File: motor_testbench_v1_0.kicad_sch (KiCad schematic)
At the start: 22 parts, among them J1 Conn_01x05_Pin, J2 Conn_01x01_Pin, J3 Conn_01x01_Pin, J4 Conn_01x22_Pin, U1 ESP32-S3-DevKitC

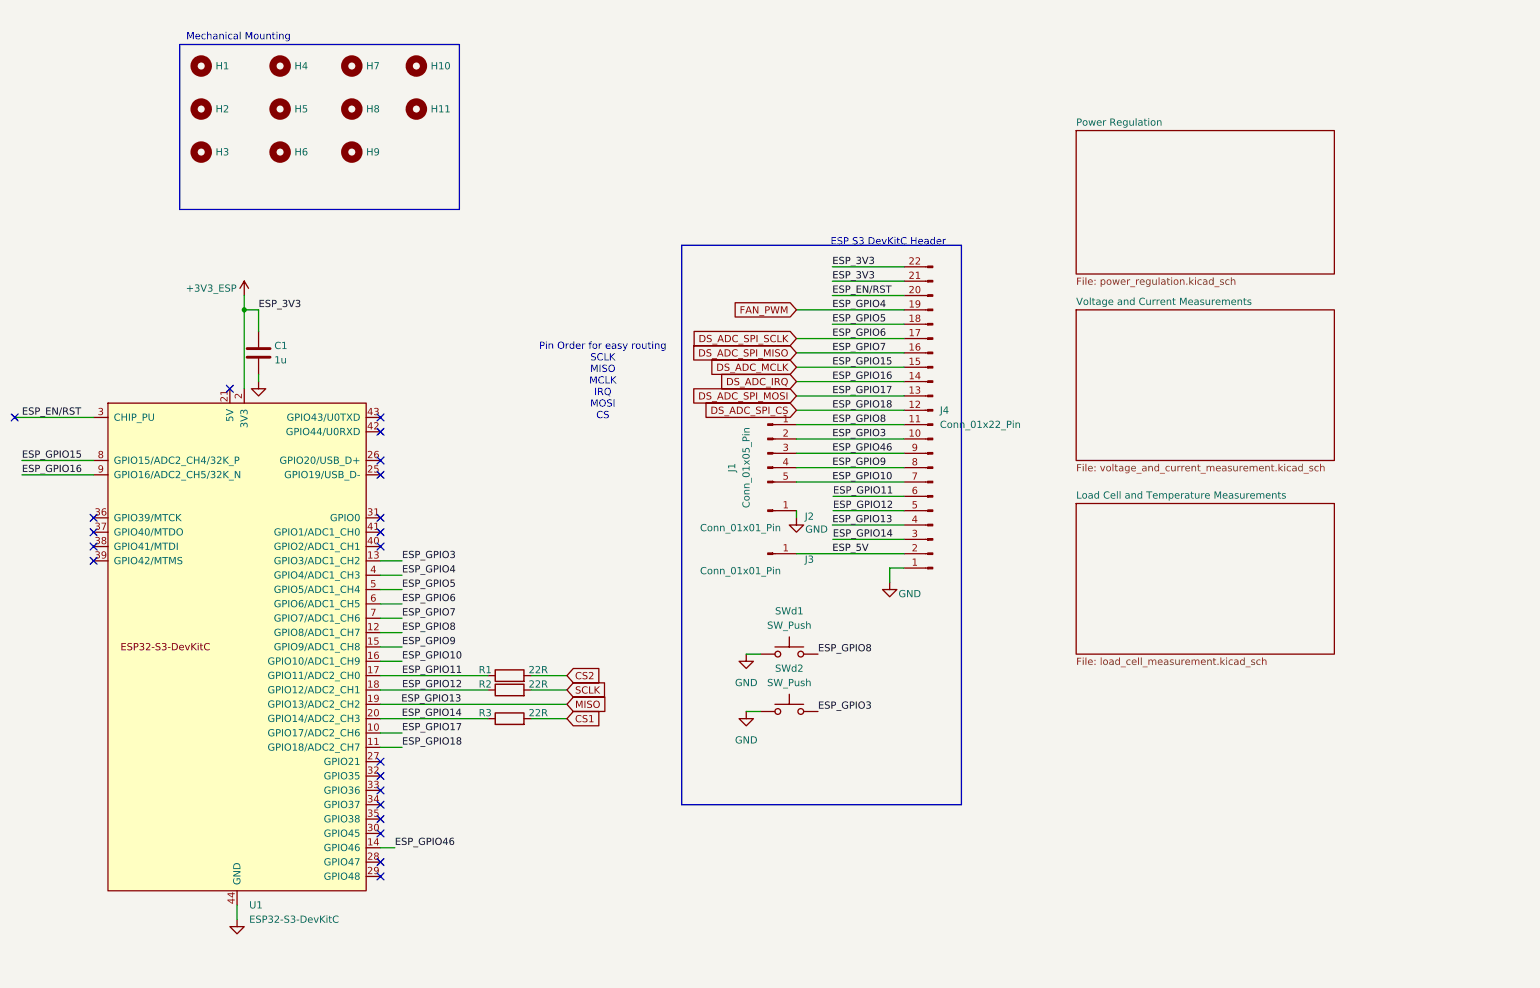
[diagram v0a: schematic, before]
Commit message: Implemented SAR ADC Buffering on top layer with one OPA387
[KiCad Version: 10.0.4]
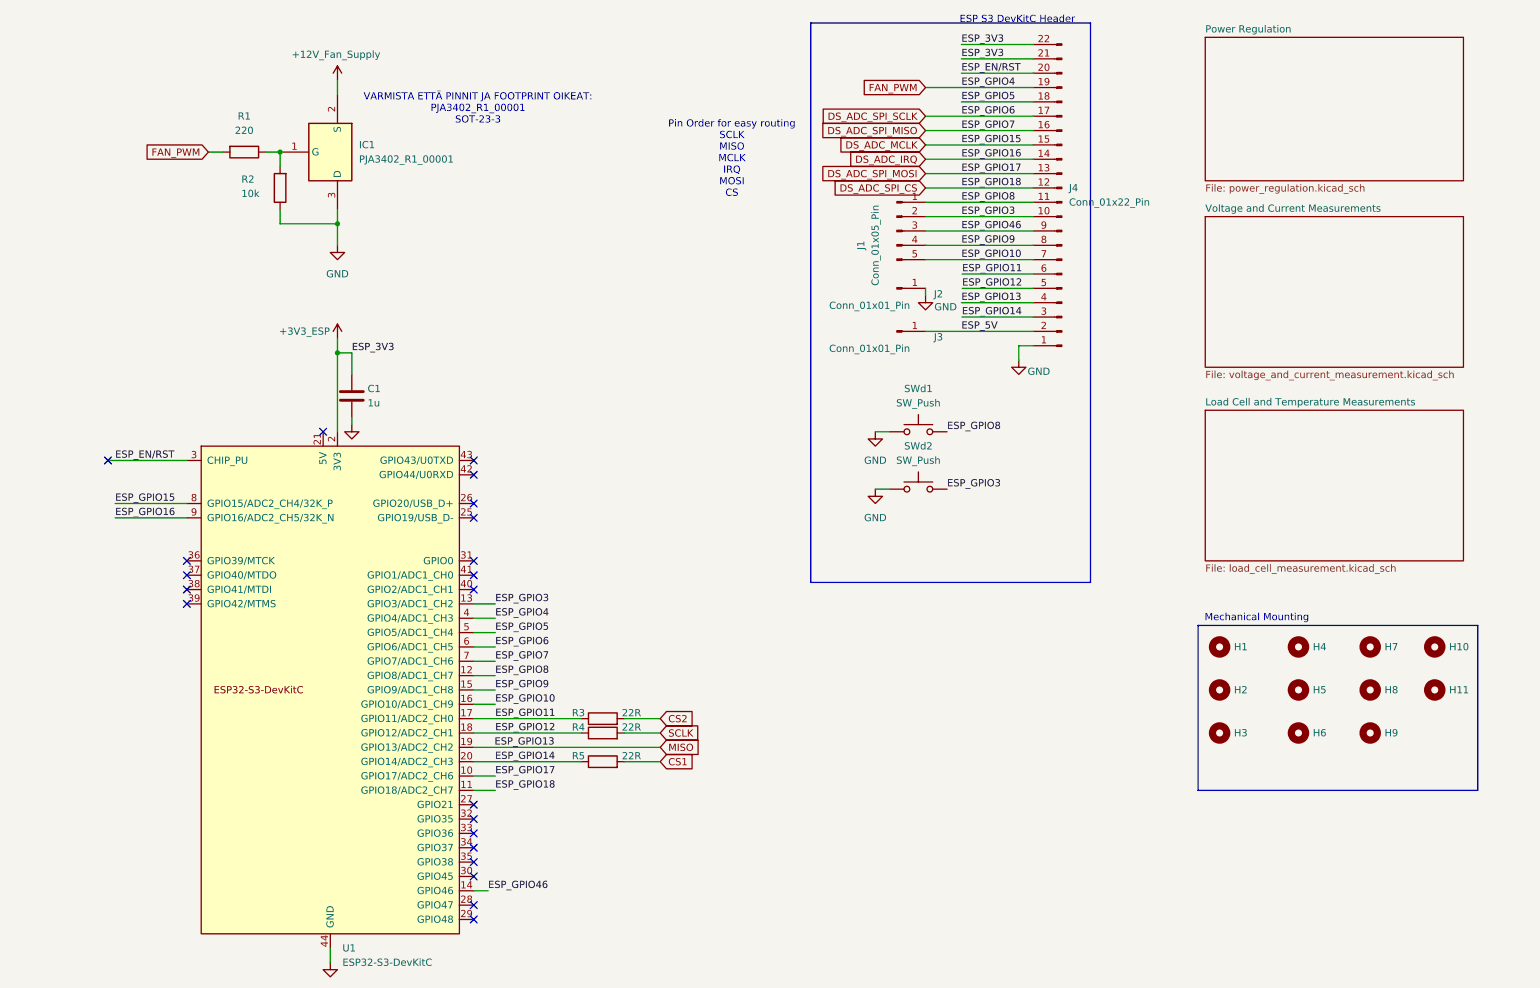
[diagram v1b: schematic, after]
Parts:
- added IC1: PJA3402_R1_00001, SOT95P240X110-3N, symbol SamacSys_Parts:PJA3402_R1_00001
- added R1: 220, Resistor_SMD:R_0603_1608Metric_Pad0.98x0.95mm_HandSolder, symbol Device:R
- added R2: 10k, Resistor_SMD:R_0603_1608Metric_Pad0.98x0.95mm_HandSolder, symbol Device:R
- renumbered R1 to R3, R2 to R4, R3 to R5
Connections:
- net FAN_PWM: now also R1.2
- net GND: now also IC1.3 (D), R2.1
- new net: IC1.1 (G), R1.1, R2.2
- new net +12V_Fan_Supply: IC1.2 (S)
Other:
- note added: "VARMISTA ETTÄ PINNIT JA FOOTPRINT OIKEAT: PJA3402_R1_00001 SOT-23-3"
- moved on the sheet: C1, H1, H10, H11, H2, H3, H4, H5, H6, H7, H8, H9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

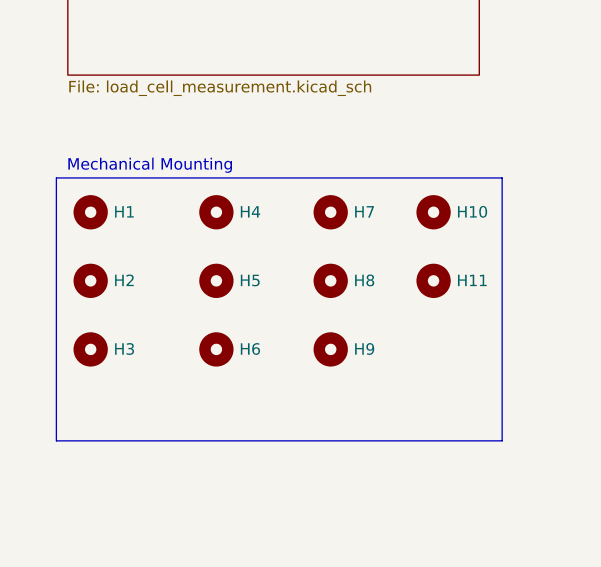
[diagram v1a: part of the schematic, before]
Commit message: Add Shutdown Protection Diodes between Power Stages
[KiCad Version: 10.0.4]
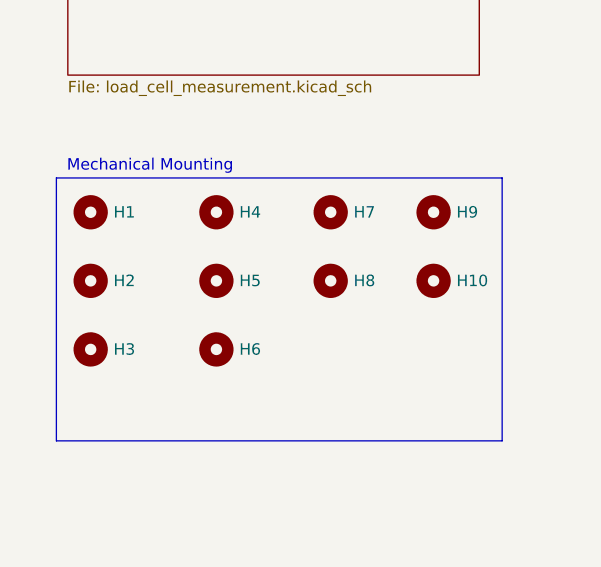
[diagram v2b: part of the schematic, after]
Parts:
- removed H4: MountingHole, MountingHole:MountingHole_2.2mm_M2_DIN965, symbol Mechanical:MountingHole
- renumbered H11 to H10, H9 to H4, H10 to H9
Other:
- moved on the sheet: H4
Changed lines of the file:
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@@
 		(in_pos_files yes)
 		(dnp no)
-		(property "Reference" "H11"
+		(property "Reference" "H10"
 			(at 275.59 137.16 0)
 			(show_name no)
@@
 			(project "motor_testbench_v1_0"
 				(path "/da638649-102c-44f9-b928-e91cd399cc2f"
-					(reference "H11")
+					(reference "H10")
 					(unit 1)
 				)
@@
 		(in_pos_files yes)
 		(dnp no)
-		(property "Reference" "H10"
+		(property "Reference" "H9"
 			(at 275.59 129.54 0)
 			(show_name no)
@@
 			(project "motor_testbench_v1_0"
 				(path "/da638649-102c-44f9-b928-e91cd399cc2f"
-					(reference "H10")
+					(reference "H9")
 					(unit 1)
 				)
@@
 					(unit 1)
 				)
-			)
-		)
-	)
-	(symbol
-		(lib_id "Mechanical:MountingHole")
-		(at 261.62 144.78 0)
-		(unit 1)
-		(body_style 1)
-		(exclude_from_sim no)
-		(in_bom no)
-		(on_board yes)
-		(in_pos_files yes)
-		(dnp no)
-		(property "Reference" "H9"
-			(at 264.16 144.78 0)
-			(show_name no)
-			(do_not_autoplace no)
-			(effects
-				(font
-					(size 1.27 1.27)
-				)
-				(justify left)
-			)
-		)
-		(property "Value" "MountingHole"
-			(at 264.16 146.0499 0)
-			(hide yes)
-			(show_name no)
-			(do_not_autoplace no)
-			(effects
-				(font
-					(size 1.27 1.27)
-				)
-				(justify left)
-			)
-		)
-		(property "Footprint" "MountingHole:MountingHole_2.2mm_M2_DIN965"
-			(at 261.62 144.78 0)
-			(hide yes)
-			(show_name no)
-			(do_not_autoplace no)
-			(effects
-				(font
-					(size 1.27 1.27)
-				)
-			)
-		)
-		(property "Datasheet" ""
-			(at 261.62 144.78 0)
-			(hide yes)
-			(show_name no)
-			(do_not_autoplace no)
-			(effects
-				(font
-					(size 1.27 1.27)
-				)
-			)
-		)
-		(property "Description" "Mounting Hole without connection"
-			(at 261.62 144.78 0)
-			(hide yes)
-			(show_name no)
-			(do_not_autoplace no)
-			(effects
-				(font
-					(size 1.27 1.27)
-				)
-			)
-		)
-		(property "Manufacturing_Number" ""
-			(at 261.62 144.78 0)
-			(hide yes)
-			(show_name no)
-			(do_not_autoplace no)
-			(effects
-				(font
-					(size 1.27 1.27)
-				)
-			)
-		)
-		(instances
-			(project "motor_testbench_v1_0"
-				(path "/da638649-102c-44f9-b928-e91cd399cc2f"
-					(reference "H9")
-					(unit 1)
-				)

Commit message: Minor Tweaks.
[KiCad Version: 10.0.4]
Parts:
- added C2: 1u, Capacitor_SMD:C_0603_1608Metric_Pad1.08x0.95mm_HandSolder, symbol Device:C
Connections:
- net +3V3_ESP: now also C2.1
- net GND: now also C2.2
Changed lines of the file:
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@@
 		(color 0 0 0 0)
 	)
+	(junction
+		(at 81.28 77.47)
+		(diameter 0)
+		(color 0 0 0 0)
+	)
 	(no_connect
 		(at 102.87 175.26)
@@
 	(wire
 		(pts
+			(xy 88.9 88.9) (xy 88.9 90.17)
+		)
+		(stroke
+			(width 0)
+			(type default)
+		)
+	)
+	(wire
+		(pts
 			(xy 173.99 91.44) (xy 176.53 91.44)
 		)
@@
 	(wire
 		(pts
+			(xy 88.9 77.47) (xy 88.9 81.28)
+		)
+		(stroke
+			(width 0)
+			(type default)
+		)
+	)
+	(wire
+		(pts
 			(xy 102.87 121.92) (xy 106.68 121.92)
 		)
@@
 	(wire
 		(pts
+			(xy 81.28 77.47) (xy 88.9 77.47)
+		)
+		(stroke
+			(width 0)
+			(type default)
+		)
+	)
+	(wire
+		(pts
 			(xy 189.3177 71.12) (xy 201.93 71.12)
 		)
@@
 		(dnp no)
 		(fields_autoplaced yes)
-		(property "Reference" "#PWR07"
+		(property "Reference" "#PWR08"
 			(at 173.99 107.95 0)
 			(hide yes)
@@
 			(project "motor_testbench_v1_0"
 				(path "/da638649-102c-44f9-b928-e91cd399cc2f"
-					(reference "#PWR07")
+					(reference "#PWR08")
+					(unit 1)
+				)
+			)
+		)
+	)
+	(symbol
+		(lib_id "Device:C")
+		(at 88.9 85.09 0)
+		(unit 1)
+		(body_style 1)
+		(exclude_from_sim no)
+		(in_bom yes)
+		(on_board yes)
+		(in_pos_files yes)
+		(dnp no)
+		(property "Reference" "C2"
+			(at 91.694 83.82 0)
+			(show_name no)
+			(do_not_autoplace no)
+			(effects
+				(font
+					(size 1.27 1.27)
+				)
+				(justify left)
+			)
+		)
+		(property "Value" "1u"
+			(at 91.694 86.36 0)
+			(show_name no)
+			(do_not_autoplace no)
+			(effects
+				(font
+					(size 1.27 1.27)
+				)
+				(justify left)
+			)
+		)
+		(property "Footprint" "Capacitor_SMD:C_0603_1608Metric_Pad1.08x0.95mm_HandSolder"
+			(at 89.8652 88.9 0)
+			(hide yes)
+			(show_name no)
+			(do_not_autoplace no)
+			(effects
+				(font
+					(size 1.27 1.27)
+				)
+			)
+		)
+		(property "Datasheet" ""
+			(at 88.9 85.09 0)
+			(hide yes)
+			(show_name no)
+			(do_not_autoplace no)
+			(effects
+				(font
+					(size 1.27 1.27)
+				)
+			)
+		)
+		(property "Description" "Unpolarized capacitor"
+			(at 88.9 85.09 0)
+			(hide yes)
+			(show_name no)
+			(do_not_autoplace no)
+			(effects
+				(font
+					(size 1.27 1.27)
+				)
+			)
+		)
+		(property "Manufacturing_Number" ""
+			(at 88.9 85.09 0)
+			(hide yes)
+			(show_name no)
+			(do_not_autoplace no)
+			(effects
+				(font
+					(size 1.27 1.27)
+				)
+			)
+		)
+		(pin "2"
+		)
+		(pin "1"
+		)
+		(instances
+			(project "motor_testbench_v1_0"
+				(path "/da638649-102c-44f9-b928-e91cd399cc2f"
+					(reference "C2")
 					(unit 1)
 				)
@@
 		(in_pos_files yes)
 		(dnp no)
-		(property "Reference" "#PWR09"
+		(property "Reference" "#PWR010"
 			(at 199.39 85.09 0)
 			(hide yes)
@@
 			(project "motor_testbench_v1_0"
 				(path "/da638649-102c-44f9-b928-e91cd399cc2f"
-					(reference "#PWR09")
+					(reference "#PWR010")
 					(unit 1)
 				)
@@
 		(in_pos_files yes)
 		(dnp no)
-		(property "Reference" "#PWR08"
+		(property "Reference" "#PWR09"
 			(at 182.88 73.66 0)
 			(hide yes)
@@
 			(project "motor_testbench_v1_0"
 				(path "/da638649-102c-44f9-b928-e91cd399cc2f"
-					(reference "#PWR08")
+					(reference "#PWR09")
 					(unit 1)
 				)
@@
 		(dnp no)
 		(fields_autoplaced yes)
-		(property "Reference" "#PWR06"
+		(property "Reference" "#PWR07"
 			(at 173.99 97.79 0)
 			(hide yes)
@@
 			(project "motor_testbench_v1_0"
 				(path "/da638649-102c-44f9-b928-e91cd399cc2f"
-					(reference "#PWR06")
+					(reference "#PWR07")
 					(unit 1)
 				)
@@
 					(unit 1)
 				)
+			)
+		)
+	)
+	(symbol
+		(lib_id "power:GND")
+		(at 88.9 90.17 0)
+		(unit 1)
+		(body_style 1)
+		(exclude_from_sim no)
+		(in_bom yes)
+		(on_board yes)
+		(in_pos_files yes)
+		(dnp no)
+		(fields_autoplaced yes)
+		(property "Reference" "#PWR06"
+			(at 88.9 96.52 0)
+			(hide yes)
+			(show_name no)
+			(do_not_autoplace no)
+			(effects
+				(font
+					(size 1.27 1.27)
+				)
+			)
+		)
+		(property "Value" "GND"
+			(at 88.9 95.25 0)
+			(hide yes)
+			(show_name no)
+			(do_not_autoplace no)
+			(effects
+				(font
+					(size 1.27 1.27)
+				)
+			)
+		)
+		(property "Footprint" ""
+			(at 88.9 90.17 0)
+			(hide yes)
+			(show_name no)
+			(do_not_autoplace no)
+			(effects
+				(font
+					(size 1.27 1.27)
+				)
+			)
+		)
+		(property "Datasheet" ""
+			(at 88.9 90.17 0)
+			(hide yes)
+			(show_name no)
+			(do_not_autoplace no)
+			(effects
+				(font
+					(size 1.27 1.27)
+				)
+			)
+		)
+		(property "Description" "Power symbol creates a global label with name \"GND\" , ground"
+			(at 88.9 90.17 0)
+			(hide yes)
+			(show_name no)
+			(do_not_autoplace no)
+			(effects
+				(font
+					(size 1.27 1.27)
+				)
+			)
+		)
+		(pin "1"
+		)
+		(instances
+			(project "motor_testbench_v1_0"
+				(path "/da638649-102c-44f9-b928-e91cd399cc2f"
+					(reference "#PWR06")
+					(unit 1)
+				)

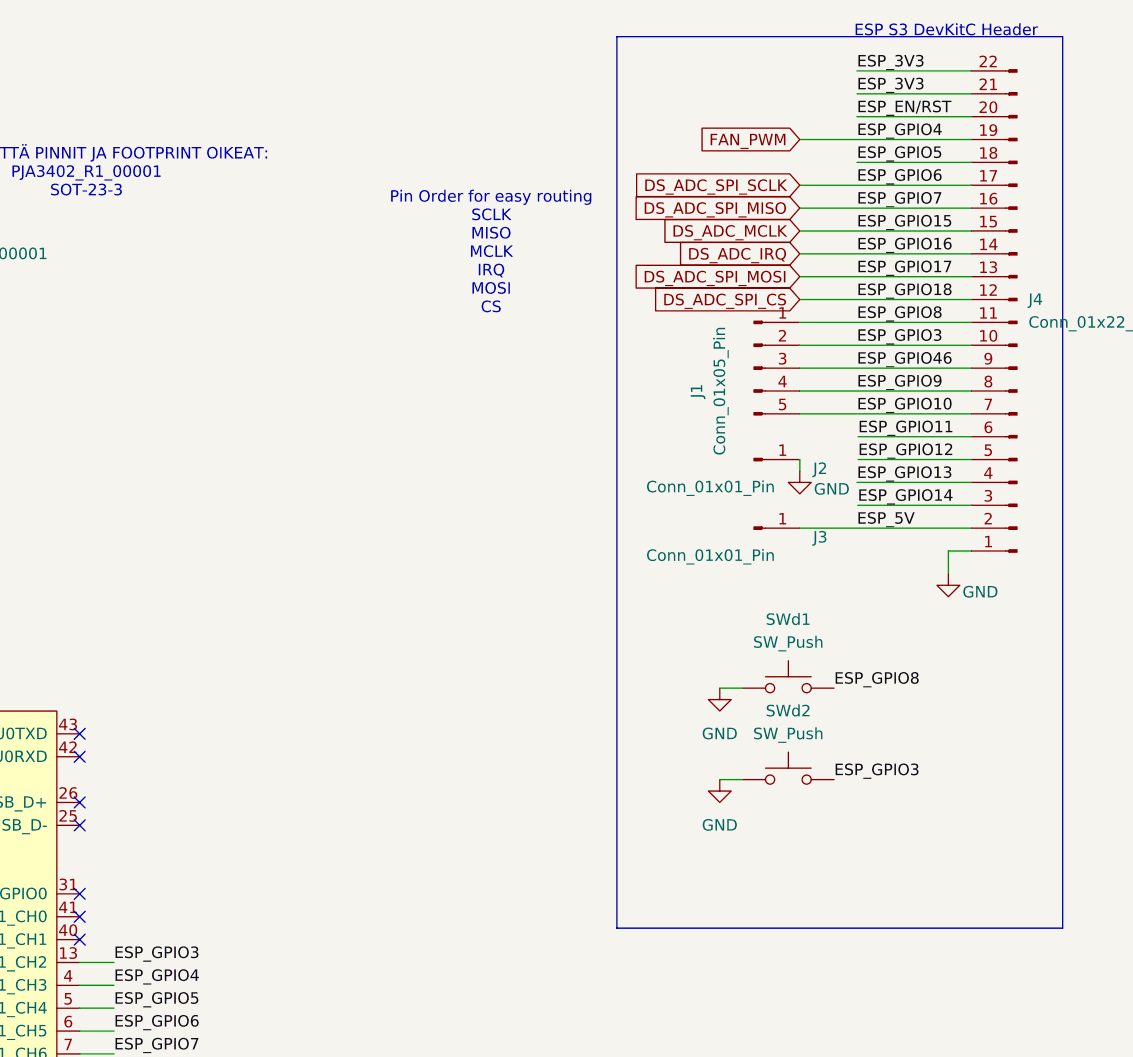
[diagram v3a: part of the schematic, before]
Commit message: Add Secondary battery voltage measurement. Minor tweaks.
[KiCad Version: 10.0.4]
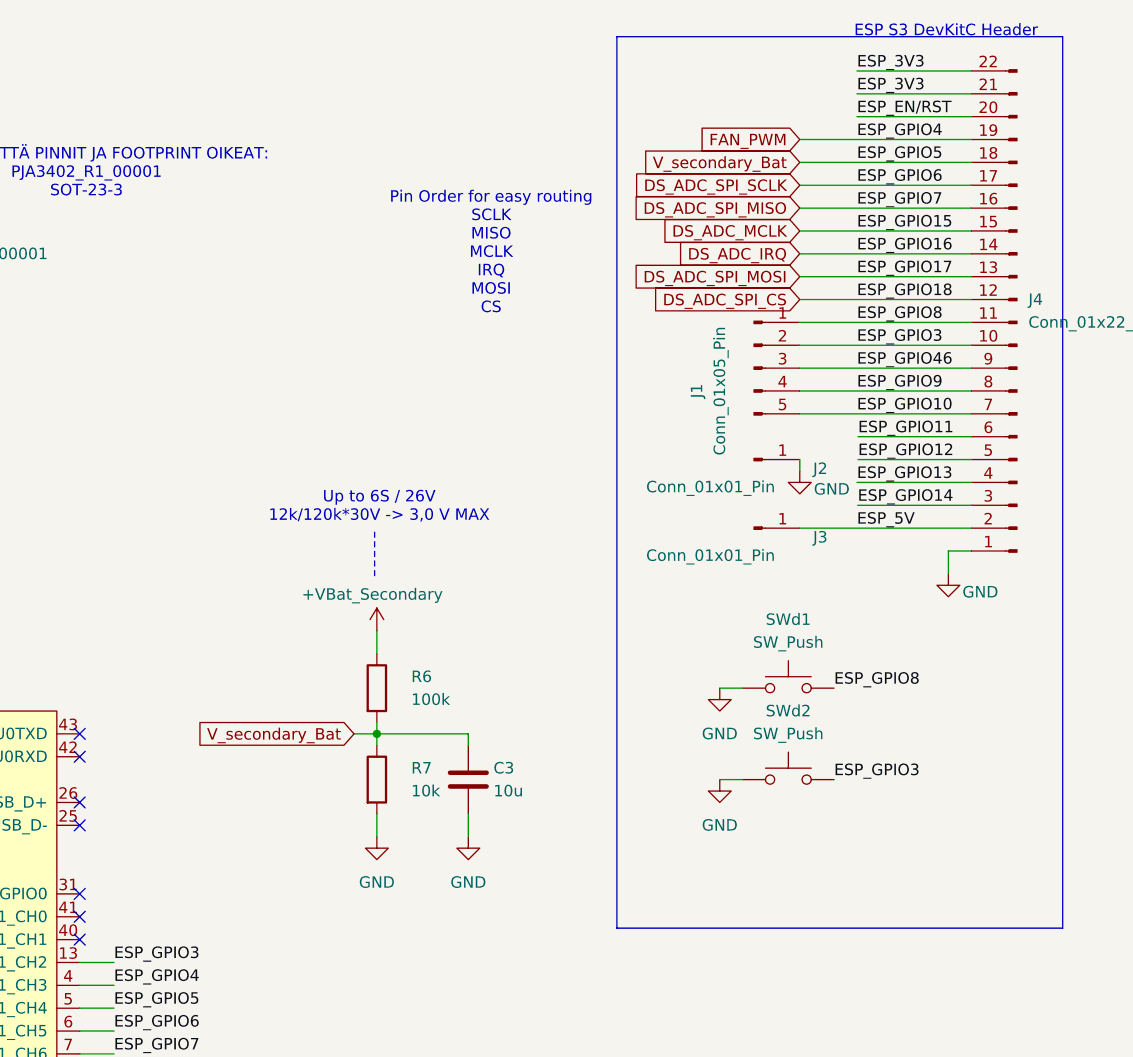
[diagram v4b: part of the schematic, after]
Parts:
- added C3: 10u, Capacitor_SMD:C_0603_1608Metric_Pad1.08x0.95mm_HandSolder, symbol Device:C
- added R6: 100k, Resistor_SMD:R_0603_1608Metric_Pad0.98x0.95mm_HandSolder, symbol Device:R
- added R7: 10k, Resistor_SMD:R_0603_1608Metric_Pad0.98x0.95mm_HandSolder, symbol Device:R
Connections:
- net GND: now also C3.2, R7.2
- net ESP_GPIO5 renamed V_secondary_Bat
- net V_secondary_Bat: now also C3.1, R6.2, R7.1
- new net +VBat_Secondary: R6.1
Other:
- note added: "Up to 6S / 26V 12k/120k*30V -> 3,0 V MAX"
